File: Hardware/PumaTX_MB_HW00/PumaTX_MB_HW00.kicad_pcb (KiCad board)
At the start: 4 copper layers, 130 x 40 mm, 106 parts, among them J100 FH12A-26S-0.5SH_55_, J101 FH12-12S-0.5SH_55_, J102 500334-0160, J103 500334-0160, J104 692122030100, J105 53398-0667, J300 U.FL-R-SMT-1_40_, J410 U.FL-R-SMT-1_40_, M130 Motor_DC, M140 Fan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

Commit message: Continued routing
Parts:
- C510, C511, C520, C521, C530, C531, R510, U510, U520, U530: moved to B.Cu
- moved R510 48.7 mm to (124.2, 103.0)
- moved C510 47.4 mm to (125.5, 103.0)
- moved U510 45.5 mm to (127.5, 103.0), turned to 180 degrees
- moved C511 43.9 mm to (129.5, 103.0)
- moved R505 43.9 mm to (175.8, 114.7), turned to -90 degrees
- moved C501 43.6 mm to (176.3, 113.0), turned to 0 degrees
- moved R504 43.3 mm to (176.8, 114.7), turned to -90 degrees
- moved R502 43.0 mm to (173.2, 112.2)
- moved R503 41.0 mm to (178.8, 112.3), turned to 0 degrees
- moved U500 38.5 mm to (176.3, 110.1), turned to 180 degrees
- moved C531 38.0 mm to (159.0, 102.5)
- moved U530 36.8 mm to (157.0, 102.5), turned to 180 degrees
- moved C530 35.9 mm to (155.0, 102.5)
- moved C502 35.4 mm to (173.4, 110.1), turned to 90 degrees
- moved C503 35.2 mm to (179.2, 110.0)
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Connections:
- D130 pad 1: /HAPTIC_HS -> /VSYS
- D140 pad 1: /FAN_HS -> /VSYS
- M130 pad 1: /HAPTIC_HS -> /VSYS
- M140 pad 1: /FAN_HS -> /VSYS
- R506 pad 1: /SYS -> /VSYS
- R507 pad 1: /SYS -> /VSYS
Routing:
- net VBUS: track 0.00 -> 114.2 mm, vias 0 -> 19
- net /BATTERY_TEMP: track 0.00 -> 22.5 mm
- net GND: track 3.25 -> 24.2 mm, vias 0 -> 14
- net /D+: track 0.00 -> 18.3 mm
- net /D-: track 0.00 -> 18.3 mm
- net /VBAT: track 0.00 -> 10.6 mm
- net /VSYS: track 2.79 -> 8.96 mm
- net /PUMATX_DTR: track 1.82 -> 7.79 mm
- net /HAPTIC_HS: track 4.35 -> 0.00 mm
- net /C2: track 7.95 -> 4.15 mm
- net /3V45: track 0.00 -> 3.53 mm
- net /SYSOFF: track 0.00 -> 2.88 mm
- net /TMR: track 0.00 -> 2.85 mm
- net /BQ_CE: track 0.00 -> 2.15 mm
- net /ILIM: track 0.00 -> 2.03 mm
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- added copper zone on F.Cu, net /FAN_LS
- added copper zone on F.Cu, net /VSYS
- added copper zone on F.Cu, net GND
- added copper zone on In1.Cu, net GND
- added copper zone on F.Cu, net VBUS

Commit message: quick esp32 update
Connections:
- U300 pad 49: (no net) -> GND
- U400 pad 49: (no net) -> GND
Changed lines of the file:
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@@
     (property "Sheetname" "")
     (attr smd)
-    (fp_text reference "U300" (at -0.341 0.132 135) (layer "B.SilkS")
-      (effects (font (size 1.27 1.27) (thickness 0.254)) (justify mirror))
-    )
-    (fp_text value "ESP32-PICO-D4" (at -0.341 0.132 135) (layer "B.SilkS") hide
-      (effects (font (size 1.27 1.27) (thickness 0.254)) (justify mirror))
-    )
-    (fp_text user "${REFERENCE}" (at -0.341 0.132 135) (layer "B.Fab")
+    (fp_text reference "U300" (at -0.341 0.132 315) (layer "B.SilkS")
+      (effects (font (size 1.27 1.27) (thickness 0.254)) (justify mirror))
+    )
+    (fp_text value "ESP32-PICO-D4" (at -0.341 0.132 315) (layer "B.SilkS") hide
+      (effects (font (size 1.27 1.27) (thickness 0.254)) (justify mirror))
+    )
+    (fp_text user "${REFERENCE}" (at -0.341 0.132 315) (layer "B.Fab")
       (effects (font (size 1.27 1.27) (thickness 0.254)) (justify mirror))
     )
     (fp_circle (center -3.991 2.825) (end -3.991 2.78788) (layer "B.SilkS") (width 0.2) (fill none))
-    (fp_line (start -3.5 -3.5) (end -3.5 3.5) (layer "B.Fab") (width 0.2))
     (fp_line (start -3.5 3.5) (end 3.5 3.5) (layer "B.Fab") (width 0.2))
     (fp_line (start 3.5 3.5) (end 3.5 -3.5) (layer "B.Fab") (width 0.2))
     (fp_line (start 3.5 -3.5) (end -3.5 -3.5) (layer "B.Fab") (width 0.2))
+    (fp_line (start -3.5 -3.5) (end -3.5 3.5) (layer "B.Fab") (width 0.2))
     (pad "1" smd rect (at -3.3 2.75 45) (size 0.35 0.55) (layers "B.Cu" "B.Paste" "B.Mask")
       (net 2 "+3V3") (pinfunction "VDDA") (pintype "power_in"))
@@
     (pad "48" smd rect (at -2.75 3.3 135) (size 0.35 0.55) (layers "B.Cu" "B.Paste" "B.Mask")
       (net 81 "unconnected-(U300-Pad48)") (pinfunction "CAP1") (pintype "bidirectional+no_connect"))
-    (pad "49" smd rect (at -0.006 0.013 45) (size 5.5 5.5) (layers "B.Cu" "B.Paste" "B.Mask"))
+    (pad "49" smd rect (at -0.006 0.013 45) (size 5.5 5.5) (layers "B.Cu" "B.Paste" "B.Mask")
+      (net 1 "GND") (pinfunction "GND") (pintype "power_in"))
     (model "C:/Users/Nico/Desktop/Component_lib/Hardware/SamacSys_Parts.3dshapes/ESP32-PICO-V3.stp"
       (offset (xyz 0 0 0))
@@
     (property "Sheetname" "")
     (attr smd)
-    (fp_text reference "U400" (at -0.341 0.132) (layer "B.SilkS")
-      (effects (font (size 1.27 1.27) (thickness 0.254)) (justify mirror))
-    )
-    (fp_text value "ESP32-PICO-D4" (at -0.341 0.132) (layer "B.SilkS") hide
-      (effects (font (size 1.27 1.27) (thickness 0.254)) (justify mirror))
-    )
-    (fp_text user "${REFERENCE}" (at -0.341 0.132) (layer "B.Fab")
+    (fp_text reference "U400" (at -0.341 0.132 180) (layer "B.SilkS")
+      (effects (font (size 1.27 1.27) (thickness 0.254)) (justify mirror))
+    )
+    (fp_text value "ESP32-PICO-D4" (at -0.341 0.132 180) (layer "B.SilkS") hide
+      (effects (font (size 1.27 1.27) (thickness 0.254)) (justify mirror))
+    )
+    (fp_text user "${REFERENCE}" (at -0.341 0.132 180) (layer "B.Fab")
       (effects (font (size 1.27 1.27) (thickness 0.254)) (justify mirror))
     )
     (fp_circle (center -3.991 2.825) (end -3.991 2.78788) (layer "B.SilkS") (width 0.2) (fill none))
+    (fp_line (start 3.5 3.5) (end 3.5 -3.5) (layer "B.Fab") (width 0.2))
     (fp_line (start -3.5 -3.5) (end -3.5 3.5) (layer "B.Fab") (width 0.2))
+    (fp_line (start 3.5 -3.5) (end -3.5 -3.5) (layer "B.Fab") (width 0.2))
     (fp_line (start -3.5 3.5) (end 3.5 3.5) (layer "B.Fab") (width 0.2))
-    (fp_line (start 3.5 -3.5) (end -3.5 -3.5) (layer "B.Fab") (width 0.2))
-    (fp_line (start 3.5 3.5) (end 3.5 -3.5) (layer "B.Fab") (width 0.2))
     (pad "1" smd rect (at -3.3 2.75 270) (size 0.35 0.55) (layers "B.Cu" "B.Paste" "B.Mask")
       (net 39 "-3V3") (pinfunction "VDDA") (pintype "power_in"))
@@
     (pad "48" smd rect (at -2.75 3.3) (size 0.35 0.55) (layers "B.Cu" "B.Paste" "B.Mask")
       (net 115 "unconnected-(U400-Pad48)") (pinfunction "CAP1") (pintype "bidirectional+no_connect"))
-    (pad "49" smd rect (at -0.006 0.013 270) (size 5.5 5.5) (layers "B.Cu" "B.Paste" "B.Mask"))
+    (pad "49" smd rect (at -0.006 0.013 270) (size 5.5 5.5) (layers "B.Cu" "B.Paste" "B.Mask")
+      (net 1 "GND") (pinfunction "GND") (pintype "power_in"))
     (model "C:/Users/Nico/Desktop/Component_lib/Hardware/SamacSys_Parts.3dshapes/ESP32-PICO-V3.stp"
       (offset (xyz 0 0 0))

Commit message: working on routing / placement
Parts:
- removed ANT400: 2450AT18A100E, Component_lib:ANTC3216X140N
- removed D500, D501: LED, Capacitor_SMD:C_0402_1005Metric
- removed J300: U.FL-R-SMT-1_40_, Component_lib:u.fl
- removed R506, R507: 1k5, Capacitor_SMD:C_0402_1005Metric
- added ANT300: 2450AT18A100E, Component_lib:ANTC3216X140N, B.Cu at (130.6, 87.1)
- added C130: 100n, Capacitor_SMD:C_0402_1005Metric, B.Cu at (194.2, 105.8)
- added C140: 100n, Capacitor_SMD:C_0402_1005Metric, F.Cu at (188.7, 113.5)
- added J400: U.FL-R-SMT-1_40_, Component_lib:u.fl, F.Cu at (183.7, 94.7)
- added R305: 120k, Capacitor_SMD:C_0402_1005Metric, B.Cu at (127.0, 96.3)
- added R306: 470k, Capacitor_SMD:C_0402_1005Metric, B.Cu at (127.0, 98.1)
- added R511: 0, Capacitor_SMD:C_0201_0603Metric, F.Cu at (155.9, 104.2)
- added R512: 0, Capacitor_SMD:C_0201_0603Metric, F.Cu at (141.8, 93.2)
- added TP105: BAT_WHITE, TestPoint:TestPoint_Pad_D1.0mm, F.Cu at (188.5, 101.5)
- added TP302: CRSF, TestPoint:TestPoint_Pad_D1.0mm, F.Cu at (152.0, 86.5)
- TP300, TP301, TP401: footprint TestPoint:TestPoint_Pad_D1.5mm -> TestPoint:TestPoint_Pad_D1.0mm
- TP400: value TestPoint -> ELRS_CHIP_PU; footprint TestPoint:TestPoint_Pad_D1.5mm -> TestPoint:TestPoint_Pad_D1.0mm
- moved TP300 33.8 mm to (126.5, 112.0)
- moved R302 23.4 mm to (122.3, 98.3), turned to 90 degrees
- moved R301 22.4 mm to (119.5, 98.3), turned to 90 degrees
- moved C301 21.4 mm to (120.4, 98.3)
- moved C302 21.4 mm to (121.4, 98.3)
- moved C300 20.8 mm to (135.5, 98.8)
- moved R300 20.8 mm to (135.5, 96.8)
- moved C306 19.2 mm to (129.1, 92.8), turned to -45 degrees
- moved L300 18.2 mm to (129.6, 91.5), turned to -135 degrees
- moved R304 18.0 mm to (116.7, 96.3), turned to 0 degrees
- moved C307 17.4 mm to (130.9, 91.0), turned to -45 degrees
- moved R303 15.8 mm to (116.7, 93.5), turned to 0 degrees
- moved C304 15.5 mm to (116.7, 95.4), turned to 180 degrees
- moved C303 15.0 mm to (116.7, 94.4), turned to 180 degrees
- moved C120 9.95 mm to (187.5, 100.8)
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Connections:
- J100 pad 10: /LED_ANODE -> /LED
- J100 pad 14: /LED_CATHODE -> GND
- U410 pad 25: (no net) -> GND
- U520 pad 4: /LED -> /AUX_EN
- U530 pad 4: /LED -> /AUX_EN
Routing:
- net VBUS: track 114.2 -> 103.5 mm, vias 19 -> 6
- net +3V3: track 2.76 -> 12.1 mm, vias 0 -> 3
- net /C1: track 0.00 -> 7.77 mm
- net /BATTERY_TEMP: track 22.5 -> 19.4 mm
- net /DISPLAY_SCL: track 0.00 -> 2.98 mm, vias 0 -> 1
- net /DISPLAY_SDA: track 0.00 -> 2.88 mm, vias 0 -> 1
- net /BATTERY_WHITE: track 0.00 -> 2.42 mm
- net /PUMATX_SDA: track 0.00 -> 1.41 mm, vias 0 -> 1
- net /PUMATX_SCL: track 0.00 -> 1.35 mm, vias 0 -> 1
- net /LEFT_POT: track 0.00 -> 1.15 mm, vias 0 -> 1
- net GND: track 24.2 -> 25.3 mm, vias 14 -> 36
- net /D-: track 18.3 -> 19.1 mm
- net /D+: track 18.3 -> 19.2 mm
- net /BQ_CE: track 2.15 -> 1.41 mm
- net /VSYS: vias 0 -> 2

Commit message: Quick update
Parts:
- moved C201 0.90 mm to (115.6, 105.5)
- moved C202 0.90 mm to (114.1, 105.5)
- moved R200 0.84 mm to (118.0, 105.3)
- moved C200 0.80 mm to (116.9, 105.5)
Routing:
- net GND: track 25.3 -> 29.7 mm, vias 36 -> 37
- net VBUS: track 103.5 -> 103.0 mm

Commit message: Routing update
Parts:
- C410, C411, C412, C413, C414, C415, C416, C419, L411, L412, L414, R511, R512: moved to B.Cu
- moved R512 18.6 mm to (156.0, 105.2), turned to 180 degrees
- moved C419 17.7 mm to (172.2, 104.8), turned to -90 degrees
- moved L414 16.3 mm to (170.1, 103.8), turned to 180 degrees
- moved C416 15.0 mm to (173.6, 104.9), turned to -90 degrees
- moved C414 13.3 mm to (174.8, 90.5)
- moved C412 13.0 mm to (176.6, 88.0), turned to 90 degrees
- moved C411 11.3 mm to (172.8, 88.2), turned to 90 degrees
- moved C410 9.93 mm to (167.8, 95.2), turned to 180 degrees
- moved C413 8.98 mm to (178.2, 90.8)
- moved L412 8.65 mm to (174.9, 92.0)
- moved L411 7.53 mm to (171.8, 90.8)
- moved C415 6.09 mm to (171.3, 94.3)
- moved C406 3.76 mm to (146.5, 92.7)
- moved Y410 0.68 mm to (174.2, 97.4), turned to 160 degrees
- moved C307 0.22 mm to (130.8, 90.8)
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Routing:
- net /VSYS: track 8.96 -> 52.3 mm, vias 2 -> 7
- net /NRESET: track 0.00 -> 9.13 mm
- net +3V3: track 12.2 -> 21.0 mm, vias 3 -> 4
- net /DIO2: track 0.00 -> 6.53 mm
- net /DIO1: track 0.00 -> 6.46 mm
- net /MISO: track 0.00 -> 6.03 mm
- net /MOSI: track 0.00 -> 5.87 mm
- net /BUSY: track 0.00 -> 5.82 mm
- net /NSS: track 0.00 -> 5.52 mm
- net /SCK: track 0.00 -> 5.41 mm
- net /50_PUMATX_ANT_1: track 0.00 -> 3.31 mm
- net /50_PUMATX_ANT_2: track 0.18 -> 2.95 mm
- net /C2: track 4.15 -> 6.88 mm
- net /XTA: track 0.00 -> 2.51 mm
- net /XTB: track 0.00 -> 2.40 mm
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- added copper zone on In2.Cu, net GND

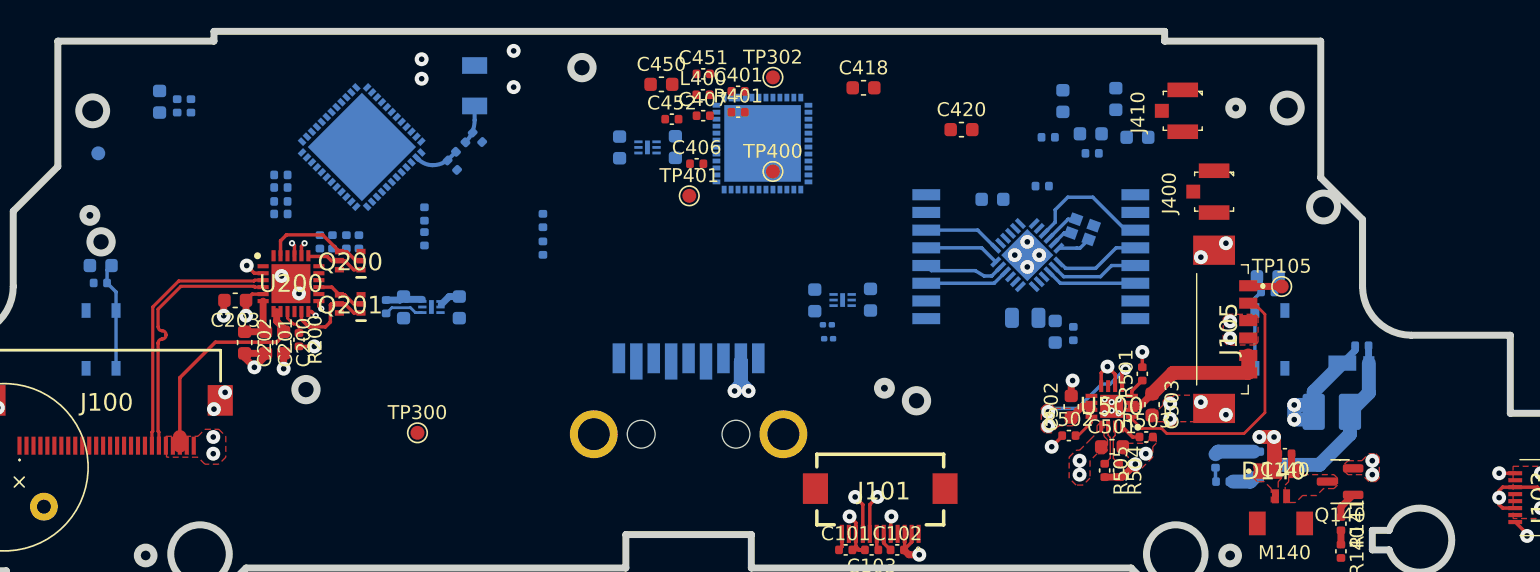
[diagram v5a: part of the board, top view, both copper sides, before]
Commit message: Done SX1280 routing and half of RF
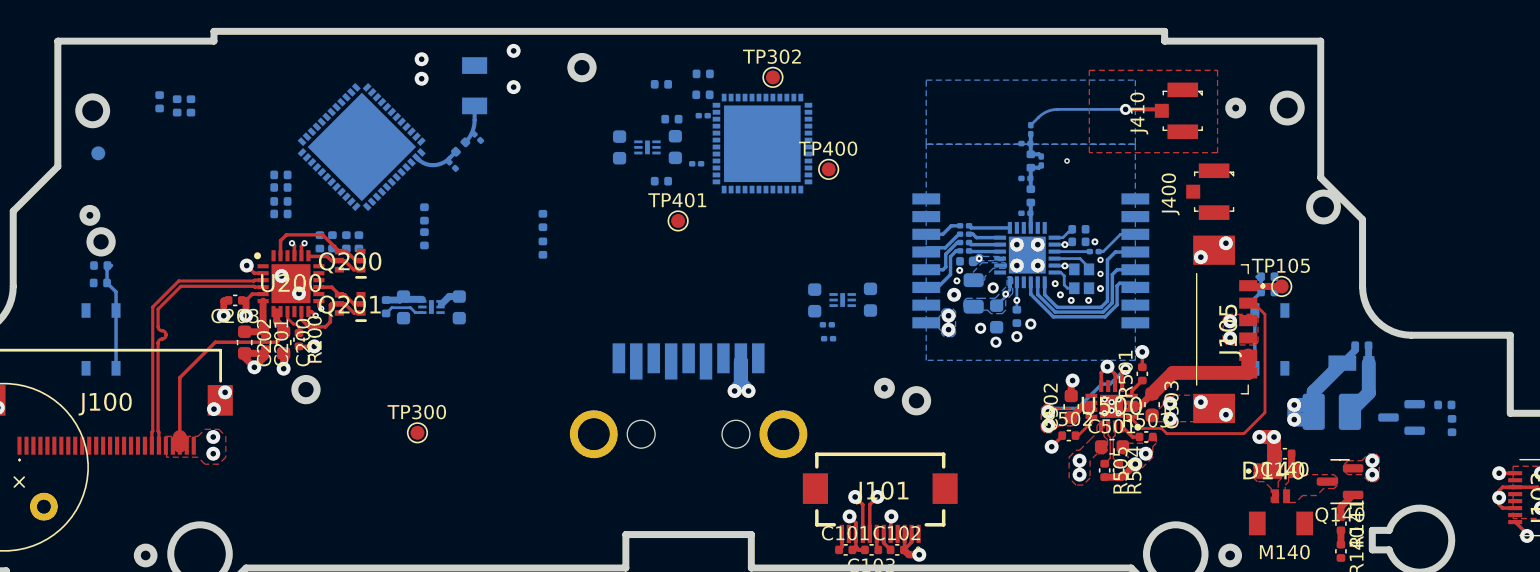
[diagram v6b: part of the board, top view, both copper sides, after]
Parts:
- added R410: 1k, Capacitor_SMD:C_0201_0603Metric, B.Cu at (165.8, 97.2)
- added R411: 1k, Capacitor_SMD:C_0201_0603Metric, B.Cu at (165.8, 97.8)
- added R412: 1k, Capacitor_SMD:C_0201_0603Metric, B.Cu at (165.8, 98.3)
- added R413: 1k, Capacitor_SMD:C_0201_0603Metric, B.Cu at (165.8, 99.0)
- added R414: 1k, Capacitor_SMD:C_0201_0603Metric, B.Cu at (175.1, 99.0)
- C110, C120, C201, C203, C350: footprint Capacitor_SMD:C_0603_1608Metric -> Capacitor_SMD:C_0402_1005Metric
- C306, C307: footprint Capacitor_SMD:C_0402_1005Metric -> Capacitor_SMD:C_0201_0603Metric
- C401, C451, C452, L400, R401: moved to B.Cu
- C406, C407: footprint Capacitor_SMD:C_0402_1005Metric -> Capacitor_SMD:C_0201_0603Metric; moved to B.Cu
- C410, C411, C412, C413, C414: footprint Capacitor_SMD:C_0603_1608Metric -> Capacitor_SMD:C_0201_0603Metric
- C418, C420, C450: footprint Capacitor_SMD:C_0603_1608Metric -> Capacitor_SMD:C_0402_1005Metric; moved to B.Cu
- moved C418 19.7 mm to (169.5, 103.7), turned to -90 degrees
- moved R130 17.2 mm to (200.7, 111.5), turned to -90 degrees
- moved R131 16.9 mm to (200.2, 110.0), turned to 0 degrees
- moved Q130 10.2 mm to (197.1, 110.9), turned to 180 degrees
- moved C420 9.46 mm to (165.9, 99.7), turned to 180 degrees
- moved C401 8.48 mm to (144.0, 94.0), turned to 180 degrees
- moved C413 7.67 mm to (170.5, 90.2), turned to 90 degrees
- moved C412 7.20 mm to (170.2, 91.2), turned to 180 degrees
- moved C416 6.59 mm to (173.9, 98.3), turned to 0 degrees
- moved C411 6.15 mm to (170.2, 93.8), turned to 180 degrees
- moved L412 4.43 mm to (170.5, 92.5), turned to 90 degrees
- moved L411 4.38 mm to (170.5, 95.0), turned to 90 degrees
- moved C419 4.34 mm to (168.1, 103.7)
- moved L414 4.09 mm to (166.4, 102.0), turned to 90 degrees
- moved C415 4.07 mm to (173.9, 97.4)
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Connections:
- U410 pad 16: /MISO -> Net-(U410-Pad16)
- U410 pad 17: /MOSI -> Net-(R412-Pad1)
- U410 pad 18: /SCK -> Net-(U410-Pad18)
- U410 pad 19: /NSS -> Net-(U410-Pad19)
- U410 pad 3: /NRESET -> Net-(U410-Pad3)
- Y410 pad 4: unconnected-(Y410-Pad4) -> GND
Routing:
- net /50_ELRS_ANT_4: track 0.00 -> 9.82 mm, vias 0 -> 1
- net /HAPTIC_LS: track 12.9 -> 5.31 mm
- net /NRESET: track 9.13 -> 3.14 mm
- net /BUSY: track 5.82 -> 11.1 mm
- net /DIO1: track 6.46 -> 10.9 mm
- net /DIO2: track 6.53 -> 10.8 mm
- net /V_DCC: track 0.00 -> 3.34 mm, vias 0 -> 2
- net Net-(U410-Pad19): track 0.00 -> 2.99 mm
- net /NSS: track 5.52 -> 2.68 mm
- net GND: track 31.2 -> 28.4 mm, vias 47 -> 65
- net /SCK: track 5.41 -> 2.84 mm
- net Net-(U410-Pad3): track 0.00 -> 2.53 mm
- net /50_ELRS_ANT_2: track 0.00 -> 2.36 mm
- net Net-(U410-Pad18): track 0.00 -> 2.33 mm
- net Net-(R412-Pad1): track 0.00 -> 2.29 mm
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- added copper zone on B.Cu, net /SX1280_3V3
- added copper zone on B.Cu, net /V_DCC
- added copper zone on B.Cu, net /V_DCC2
- added copper zone on B.Cu, net GND

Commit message: routing is ongoing
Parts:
- moved U400 5.98 mm to (155.6, 95.4), turned to -90 degrees
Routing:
- net /50_ESP_ELRS_ANT_1: vias 0 -> 1

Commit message: rf backup
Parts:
- C501, C502, C503, R501, R502, R503, R504, R505, U500: moved to B.Cu
- moved C502 31.6 mm to (203.9, 101.8), turned to 0 degrees
- moved R502 30.3 mm to (201.8, 102.0), turned to 90 degrees
- moved R501 29.8 mm to (206.2, 96.8), turned to 0 degrees
- moved U500 29.8 mm to (203.9, 99.0), turned to -90 degrees
- moved C503 28.5 mm to (204.0, 96.0), turned to 180 degrees
- moved C501 28.4 mm to (201.0, 98.9), turned to 90 degrees
- moved R505 28.0 mm to (199.3, 99.5), turned to 180 degrees
- moved R503 27.9 mm to (201.7, 96.5), turned to 90 degrees
- moved R504 27.8 mm to (199.3, 98.5), turned to 180 degrees
- moved R512 12.5 mm to (143.8, 102.7)
- moved C530 12.5 mm to (142.8, 100.0)
- moved C531 12.5 mm to (146.8, 99.9)
- moved R511 12.5 mm to (143.7, 101.7)
- moved U530 12.5 mm to (144.8, 99.9)
- moved C416 7.18 mm to (178.4, 103.9)
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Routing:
- net /VSYS: track 52.3 -> 29.3 mm
- net /BATTERY_TEMP: track 19.4 -> 3.18 mm
- net VBUS: track 103.0 -> 99.9 mm
- net /50_ELRS_ANT_4: track 9.88 -> 7.48 mm
- net /50_ESP_ELRS_ANT_2: track 0.00 -> 1.40 mm, vias 0 -> 1
- net GND: vias 65 -> 61
- added copper zone on B.Cu, net /VSYS
- added copper zone on B.Cu, net VBUS
